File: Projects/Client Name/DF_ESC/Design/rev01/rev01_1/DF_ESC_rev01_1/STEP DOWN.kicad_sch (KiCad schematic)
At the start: 38 parts, among them U1 STM32F405RGTx

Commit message: Update 2024-02-28_2
Input Proteccion Done
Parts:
- removed C1, C? (x10): 100n, symbol Device:C
- removed C? (x2): 2u2, symbol Device:C
- removed C?: 1u, symbol Device:C
- removed C?: 10u, symbol Device:C
- removed C? (x2): C, symbol Device:C
- removed D?: LED_G, symbol Device:LED
- removed D?: LED_R, symbol Device:LED
- removed D?: LED, symbol Device:LED
- removed FB?: FerriteBead, symbol Device:FerriteBead
- removed J?: Conn_01x03_Pin, symbol Connector:Conn_01x03_Pin
- removed J?: Conn_01x08_Pin, symbol Connector:Conn_01x08_Pin
- removed J?: Conn_01x06_Pin, symbol Connector:Conn_01x06_Pin
- removed R1, R2, R?: 1k, symbol Device:R
- removed R3, R? (x2): 2k2, symbol Device:R
- removed R?: 39k, symbol Device:R
- removed R?: 0R, symbol Device:R
- removed R? (x2): R, symbol Device:R
- removed SW?: SW_DIP_x01, symbol Switch:SW_DIP_x01
- removed TH?: 10k, symbol Device:Thermistor_NTC
- removed U1: STM32F405RGTx, Package_QFP:LQFP-64_10x10mm_P0.5mm, symbol MCU_ST_STM32F4:STM32F405RGTx
- removed Y?: Crystal_Small, symbol Device:Crystal_Small
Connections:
- no-connect marks 18 -> 0
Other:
- note added: "[3] - STEP-DOWN"
- note removed: "100nF Decoupling capacitors. Place one as close as possible to each pin"
- note removed: "COMMUNICATION"
- note removed: "NRST internally pulled-up"
- note removed: "NTC THERMISTOR"
- note removed: "PROG/DEBUG"
- note removed: "SERVO"
- note removed: "Set Boot mode Table 7"
- note removed: "Subtitute with 100R If used as servo output"
- note removed: "VOLTAGE_DIVIDER"
- note removed: "WHEN: VDC = 60V => AN_IN = 3V204"
- note removed: "[3] - MCU"

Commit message: update 2024-02-29
CAN Page DONE
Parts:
- added C2, C3, C6, C7: 1u, symbol Device:C
- added D1, D2: LED_G, symbol Device:LED
- added D3: BAT60A, Diode_SMD:D_SOD-323, symbol Diode:BAT60A
- added R2, R3: R, symbol Device:R
- added U2: AMS1117-3.3, Package_TO_SOT_SMD:SOT-223-3_TabPin2, symbol Regulator_Linear:AMS1117-3.3
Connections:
- new net: D1.2 (A), R2.2
- new net: D2.2 (A), R3.2
- new net +3V3: C2.1, C3.1, D3.1 (K), R2.1, R3.1, U2.3 (VI)
- new net +3V3_IC: C6.1, C7.1, D3.2 (A), U2.2 (VO)
- new net GND: C2.2, C3.2, C6.2, C7.2, D1.1 (K), D2.1 (K), U2.1 (GND)
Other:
- note added: "FROM MOSFET DRIVER OR EXTERNAL"

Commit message: Update 2024-02-03
Schematic finish but DRC CHEK Errors
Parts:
- C5: renamed from C2; footprint (none) -> Capacitor_SMD:C_0603_1608Metric_Pad1.08x0.95mm_HandSolder
- C6: renamed from C3; footprint (none) -> Capacitor_SMD:C_0603_1608Metric_Pad1.08x0.95mm_HandSolder
- C7: renamed from C6; footprint (none) -> Capacitor_SMD:C_0603_1608Metric_Pad1.08x0.95mm_HandSolder
- C8: renamed from C7; footprint (none) -> Capacitor_SMD:C_0603_1608Metric_Pad1.08x0.95mm_HandSolder
- D3: renamed from D1; footprint (none) -> LED_SMD:LED_1206_3216Metric_Pad1.42x1.75mm_HandSolder
- D5: renamed from D2; footprint (none) -> LED_SMD:LED_1206_3216Metric_Pad1.42x1.75mm_HandSolder
- R5: renamed from R2; value R -> 1k; footprint (none) -> Resistor_SMD:R_0603_1608Metric_Pad0.98x0.95mm_HandSolder
- R6: renamed from R3; value R -> 1k; footprint (none) -> Resistor_SMD:R_0603_1608Metric_Pad0.98x0.95mm_HandSolder
- renumbered D3 to D4

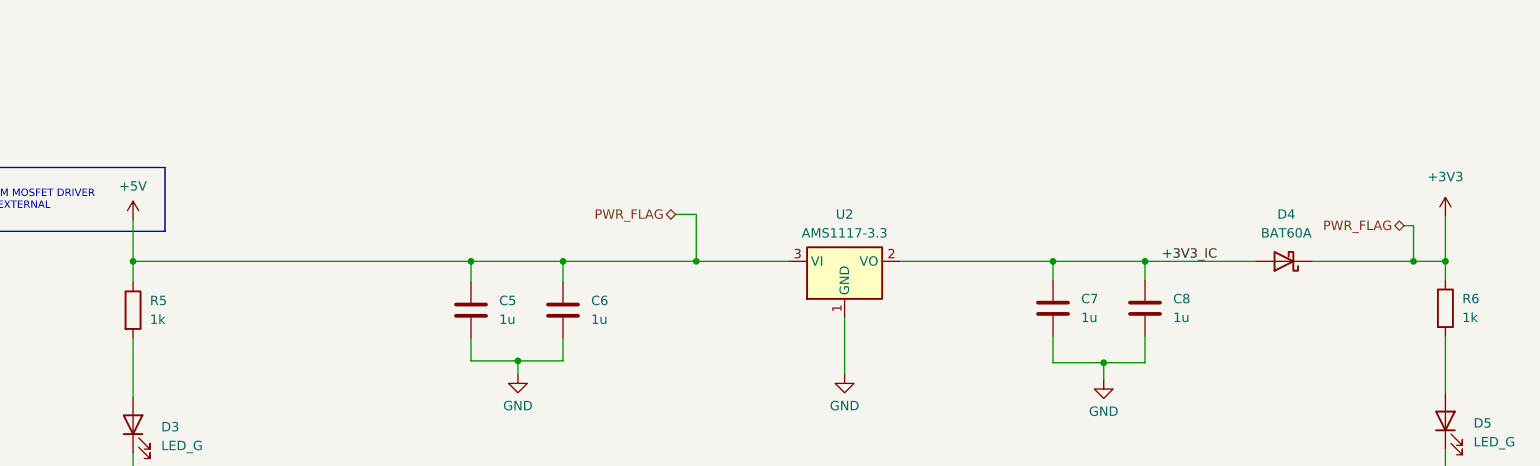
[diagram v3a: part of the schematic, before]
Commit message: Update 2024-03-03
ERC 0 Errors. Update PCB from schematics prepare to going on
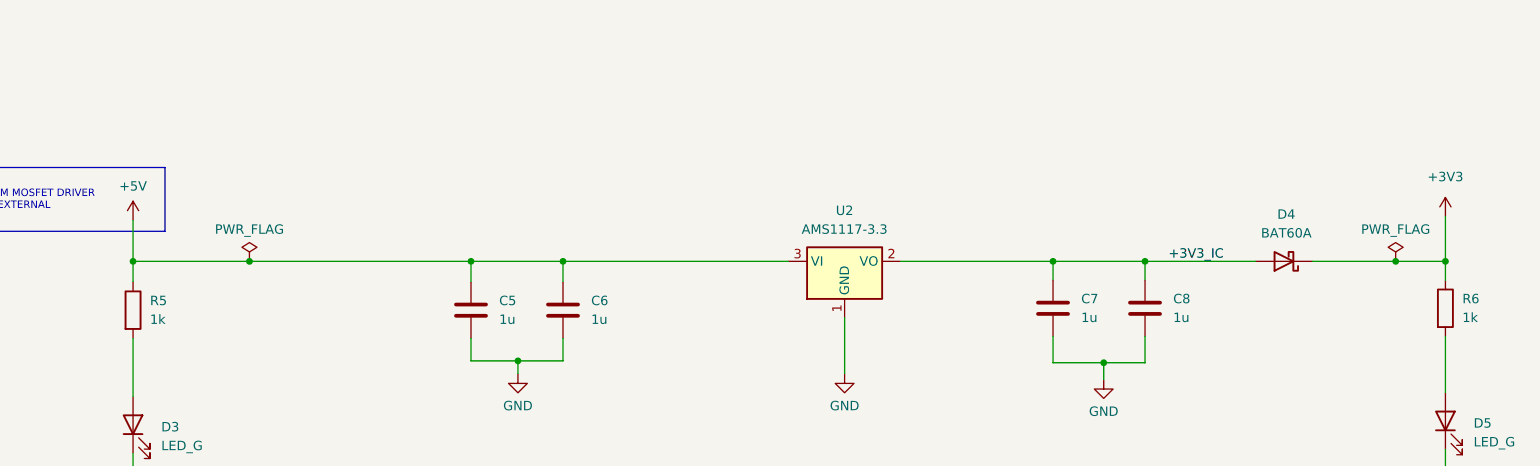
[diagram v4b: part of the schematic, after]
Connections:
- net +3V3: no longer C5.1, C6.1, R5.1, U2.3 (VI)
- new net +5V: C5.1, C6.1, R5.1, U2.3 (VI)
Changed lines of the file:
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@@
   (junction (at 191.516 92.964) (diameter 0) (color 0 0 0 0)
   )
-  (junction (at 136.398 79.248) (diameter 0) (color 0 0 0 0)
-  )
-  (junction (at 233.426 79.248) (diameter 0) (color 0 0 0 0)
-  )
   (junction (at 184.658 79.248) (diameter 0) (color 0 0 0 0)
   )
@@
   (junction (at 197.104 79.248) (diameter 0) (color 0 0 0 0)
   )
+  (junction (at 231.013 79.248) (diameter 0) (color 0 0 0 0)
+  )
   (junction (at 237.744 79.248) (diameter 0) (color 0 0 0 0)
   )
@@
   (junction (at 112.268 92.71) (diameter 0) (color 0 0 0 0)
   )
+  (junction (at 75.946 79.248) (diameter 0) (color 0 0 0 0)
+  )
   (junction (at 105.918 79.248) (diameter 0) (color 0 0 0 0)
   )
@@
     (stroke (width 0) (type default))
   )
-  (wire (pts (xy 60.198 79.248) (xy 105.918 79.248))
+  (wire (pts (xy 60.198 79.248) (xy 75.946 79.248))
     (stroke (width 0) (type default))
   )
@@
     (stroke (width 0) (type default))
   )
-  (wire (pts (xy 118.364 79.248) (xy 136.398 79.248))
-    (stroke (width 0) (type default))
-  )
-  (wire (pts (xy 133.604 72.898) (xy 136.398 72.898))
-    (stroke (width 0) (type default))
-  )
-  (wire (pts (xy 219.71 79.248) (xy 233.426 79.248))
-    (stroke (width 0) (type default))
-  )
-  (wire (pts (xy 232.156 74.422) (xy 233.426 74.422))
+  (wire (pts (xy 118.364 79.248) (xy 148.844 79.248))
     (stroke (width 0) (type default))
   )
@@
     (stroke (width 0) (type default))
   )
+  (wire (pts (xy 75.946 79.248) (xy 105.918 79.248))
+    (stroke (width 0) (type default))
+  )
   (wire (pts (xy 60.198 105.156) (xy 60.198 108.712))
     (stroke (width 0) (type default))
@@
     (stroke (width 0) (type default))
   )
-  (wire (pts (xy 136.398 72.898) (xy 136.398 79.248))
+  (wire (pts (xy 231.013 79.248) (xy 237.744 79.248))
     (stroke (width 0) (type default))
   )
@@
     (stroke (width 0) (type default))
   )
+  (wire (pts (xy 219.71 79.248) (xy 231.013 79.248))
+    (stroke (width 0) (type default))
+  )
   (wire (pts (xy 105.918 79.248) (xy 105.918 82.042))
     (stroke (width 0) (type default))
@@
   )
   (wire (pts (xy 156.464 86.868) (xy 156.464 94.488))
-    (stroke (width 0) (type default))
-  )
-  (wire (pts (xy 233.426 74.422) (xy 233.426 79.248))
-    (stroke (width 0) (type default))
-  )
-  (wire (pts (xy 233.426 79.248) (xy 237.744 79.248))
-    (stroke (width 0) (type default))
-  )
-  (wire (pts (xy 136.398 79.248) (xy 148.844 79.248))
     (stroke (width 0) (type default))
   )
@@
     (effects (font (size 1 1)) (justify left bottom))
   )
-  (label "+3V3_IC" (at 199.39 79.248 0) (fields_autoplaced)
+  (label "+3V3_IC" (at 200.279 79.248 0) (fields_autoplaced)
     (effects (font (size 1.27 1.27)) (justify left bottom))
-  )
-  (hierarchical_label "PWR_FLAG" (shape bidirectional) (at 232.156 74.422 180) (fields_autoplaced)
-    (effects (font (size 1.27 1.27)) (justify right))
-  )
-  (hierarchical_label "PWR_FLAG" (shape bidirectional) (at 133.604 72.898 180) (fields_autoplaced)
-    (effects (font (size 1.27 1.27)) (justify right))
   )
   (symbol (lib_id "power:GND") (at 156.464 94.488 0) (unit 1)
@@
     )
   )
+  (symbol (lib_id "power:PWR_FLAG") (at 75.946 79.248 0) (unit 1)
+    (in_bom yes) (on_board yes) (dnp no) (fields_autoplaced)
+    (property "Reference" "#FLG03" (at 75.946 77.343 0)
+      (effects (font (size 1.27 1.27)) hide)
+    )
+    (property "Value" "PWR_FLAG" (at 75.946 74.93 0)
+      (effects (font (size 1.27 1.27)))
+    )
+    (property "Footprint" "" (at 75.946 79.248 0)
+      (effects (font (size 1.27 1.27)) hide)
+    )
+    (property "Datasheet" "~" (at 75.946 79.248 0)
+      (effects (font (size 1.27 1.27)) hide)
+    )
+    (pin "1")
+    (instances
+      (project "DF_ESC_rev01_1"
+        (path "/e63e39d7-6ac0-4ffd-8aa3-1841a4541b55/972ef474-8d49-43c2-822c-942f76f71b8f"
+          (reference "#FLG03") (unit 1)
+        )
+      )
+    )
+  )
   (symbol (lib_id "power:GND") (at 112.268 94.488 0) (unit 1)
     (in_bom yes) (on_board yes) (dnp no) (fields_autoplaced)
@@
         (path "/e63e39d7-6ac0-4ffd-8aa3-1841a4541b55/972ef474-8d49-43c2-822c-942f76f71b8f"
           (reference "#PWR012") (unit 1)
-        )
-      )
-    )
-  )
-  (symbol (lib_id "Regulator_Linear:AMS1117-3.3") (at 156.464 79.248 0) (unit 1)
-    (in_bom yes) (on_board yes) (dnp no) (fields_autoplaced)
-    (property "Reference" "U2" (at 156.464 72.898 0)
-      (effects (font (size 1.27 1.27)))
-    )
-    (property "Value" "AMS1117-3.3" (at 156.464 75.438 0)
-      (effects (font (size 1.27 1.27)))
-    )
-    (property "Footprint" "Package_TO_SOT_SMD:SOT-223-3_TabPin2" (at 156.464 74.168 0)
-      (effects (font (size 1.27 1.27)) hide)
-    )
-    (property "Datasheet" "http://www.advanced-monolithic.com/pdf/ds1117.pdf" (at 159.004 86.868 0)
-      (effects (font (size 1.27 1.27)) hide)
-    )
-    (pin "2")
-    (pin "1")
-    (pin "3")
-    (instances
-      (project "DF_ESC_rev01_1"
-        (path "/e63e39d7-6ac0-4ffd-8aa3-1841a4541b55/972ef474-8d49-43c2-822c-942f76f71b8f"
-          (reference "U2") (unit 1)
         )
       )
@@
     )
   )
+  (symbol (lib_id "Regulator_Linear:AMS1117-3.3") (at 156.464 79.248 0) (unit 1)
+    (in_bom yes) (on_board yes) (dnp no) (fields_autoplaced)
+    (property "Reference" "U2" (at 156.464 72.39 0)
+      (effects (font (size 1.27 1.27)))
+    )
+    (property "Value" "AMS1117-3.3" (at 156.464 74.93 0)
+      (effects (font (size 1.27 1.27)))
+    )
+    (property "Footprint" "Package_TO_SOT_SMD:SOT-223-3_TabPin2" (at 156.464 74.168 0)
+      (effects (font (size 1.27 1.27)) hide)
+    )
+    (property "Datasheet" "http://www.advanced-monolithic.com/pdf/ds1117.pdf" (at 159.004 85.598 0)
+      (effects (font (size 1.27 1.27)) hide)
+    )
+    (pin "1")
+    (pin "3")
+    (pin "2")
+    (instances
+      (project "DF_ESC_rev01_1"
+        (path "/e63e39d7-6ac0-4ffd-8aa3-1841a4541b55/972ef474-8d49-43c2-822c-942f76f71b8f"
+          (reference "U2") (unit 1)
+        )
+      )
+    )
+  )
   (symbol (lib_id "power:GND") (at 237.744 108.204 0) (unit 1)
     (in_bom yes) (on_board yes) (dnp no) (fields_autoplaced)
@@
         )
       )
+    )
+  )
+  (symbol (lib_id "power:PWR_FLAG") (at 231.013 79.248 0) (unit 1)
+    (in_bom yes) (on_board yes) (dnp no) (fields_autoplaced)
+    (property "Reference" "#FLG04" (at 231.013 77.343 0)
+      (effects (font (size 1.27 1.27)) hide)
+    )
+    (property "Value" "PWR_FLAG" (at 231.013 74.93 0)
+      (effects (font (size 1.27 1.27)))
+    )
+    (property "Footprint" "" (at 231.013 79.248 0)
+      (effects (font (size 1.27 1.27)) hide)
+    )
+    (property "Datasheet" "~" (at 231.013 79.248 0)
+      (effects (font (size 1.27 1.27)) hide)
+    )
+    (pin "1")
+    (instances
+      (project "DF_ESC_rev01_1"
+        (path "/e63e39d7-6ac0-4ffd-8aa3-1841a4541b55/972ef474-8d49-43c2-822c-942f76f71b8f"
+          (reference "#FLG04") (unit 1)
+        )
+      )
